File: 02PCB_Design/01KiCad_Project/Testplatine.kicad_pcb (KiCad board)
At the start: 4 copper layers, 210.4 x 100 mm, 137 parts, among them J1 MTSW-104-22-L-D-265-RA, J2 Screw_Terminal_01x03, J3 FCR7350R, J4 FCR7350R, J5 DE9_Receptacle_MountingHoles, J6 MTSW-104-22-L-D-265-RA, J7 Conn_01x06_Pin, U1 AS5047P-ATSM, U10 INA240A1PW, U11 NUCLEO-G431RB, U12 MCP2562FD, U2 ISM330BXTR, U3 L6982, U4 AP2114D, U5 LMG2100R044RARR, U6 INA240A1PW, U7 LMG2100R044RARR, U8 INA240A1PW, U9 LMG2100R044RARR

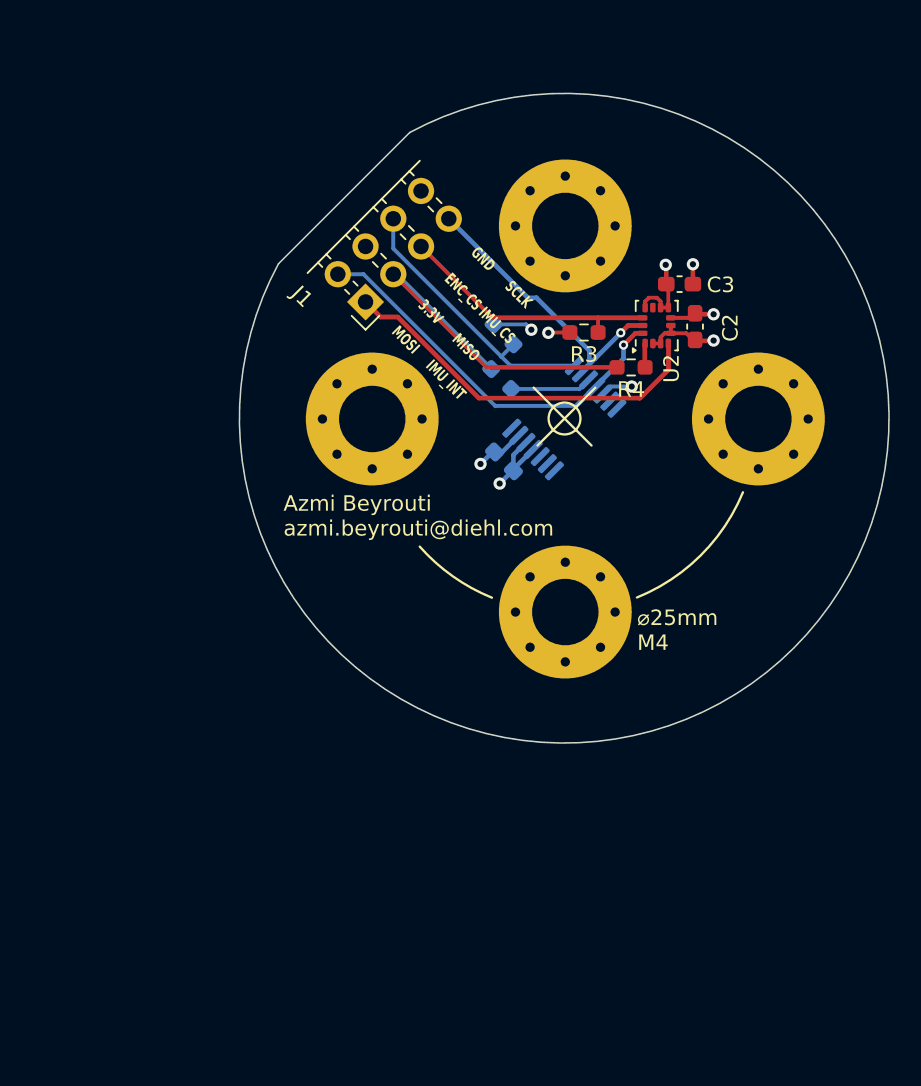
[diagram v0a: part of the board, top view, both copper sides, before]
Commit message: Changed Some Capacitor Sizes, Added Capacitors in Power Gen
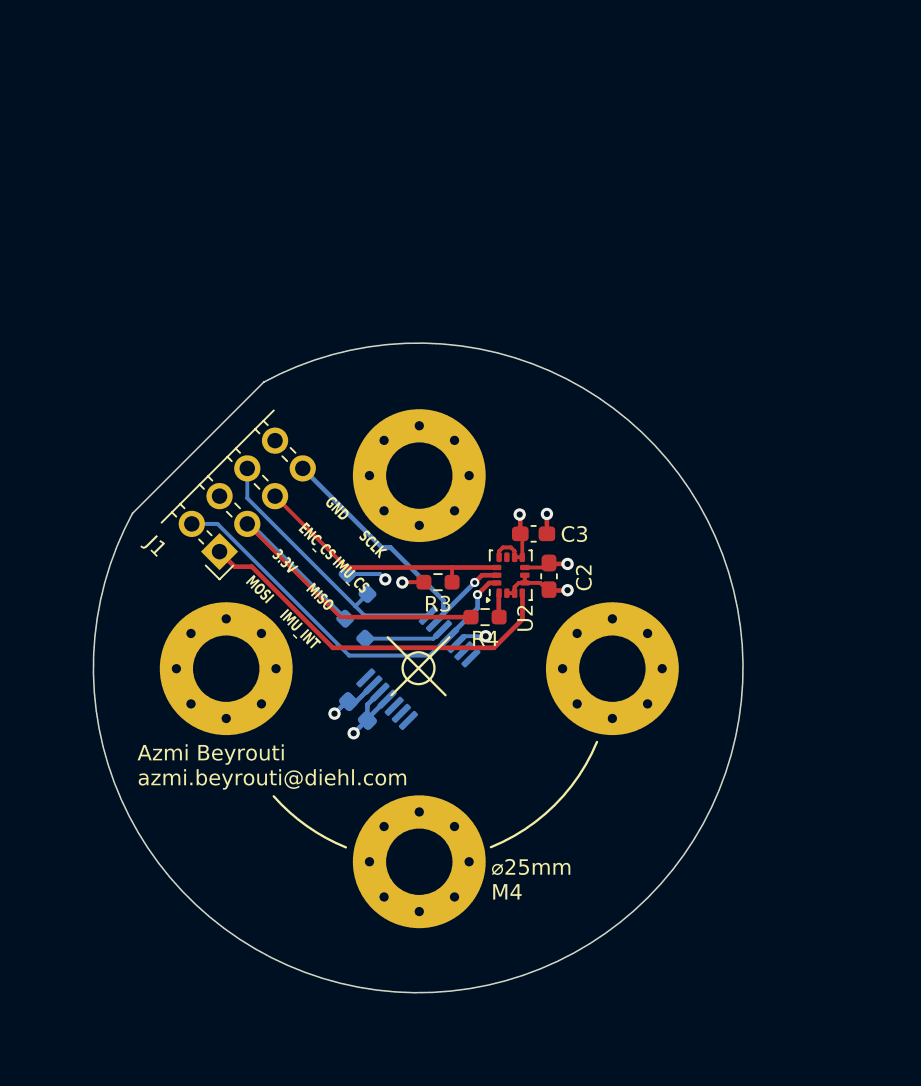
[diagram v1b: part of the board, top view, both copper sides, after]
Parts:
- moved C1 18.7 mm to (219.8, 113.0)
- moved C2 18.7 mm to (232.2, 104.3)
- moved C3 18.7 mm to (231.2, 101.6)
- moved H1 18.7 mm to (223.8, 97.8)
- moved H2 18.7 mm to (223.8, 122.8)
- moved H3 18.7 mm to (236.3, 110.3)
- moved H4 18.7 mm to (211.3, 110.3)
- moved R1 18.7 mm to (219.8, 104.8)
- moved R2 18.7 mm to (219.6, 107.7)
- moved R4 18.7 mm to (228.0, 107.0)
- moved U1 18.7 mm to (223.7, 110.2)
- moved J1 18.7 mm to (210.8, 102.7)
- moved R3 18.7 mm to (225.0, 104.7)
- moved U2 18.7 mm to (229.7, 104.2)
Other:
- board size 210.4 x 100 mm -> 201 x 100 mm

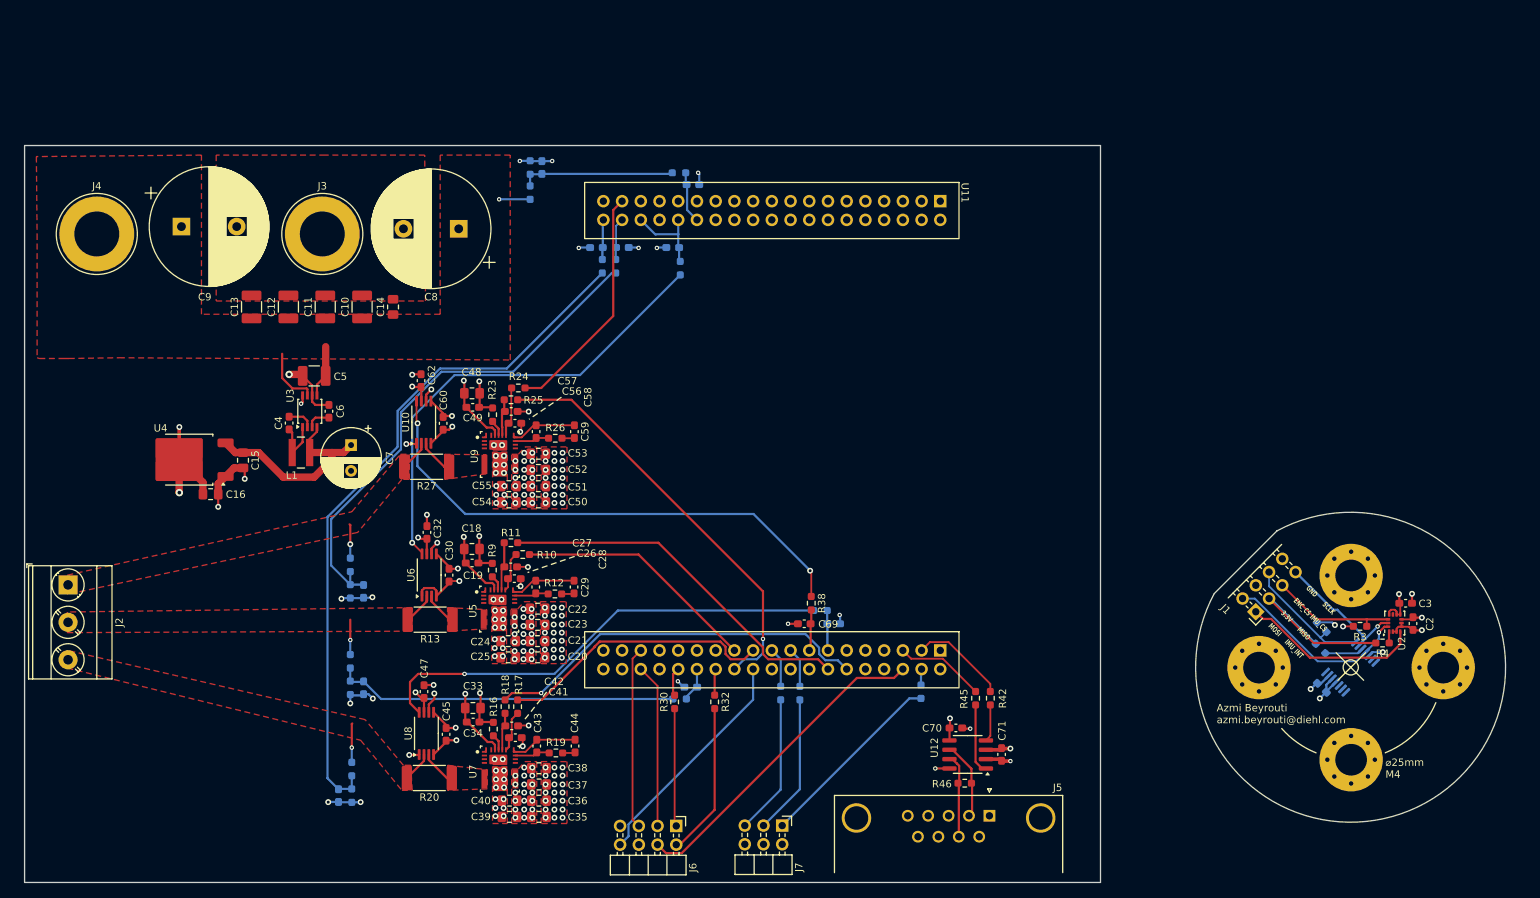
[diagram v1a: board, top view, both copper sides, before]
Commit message: Reworked Half-Bridge and Power-Gen
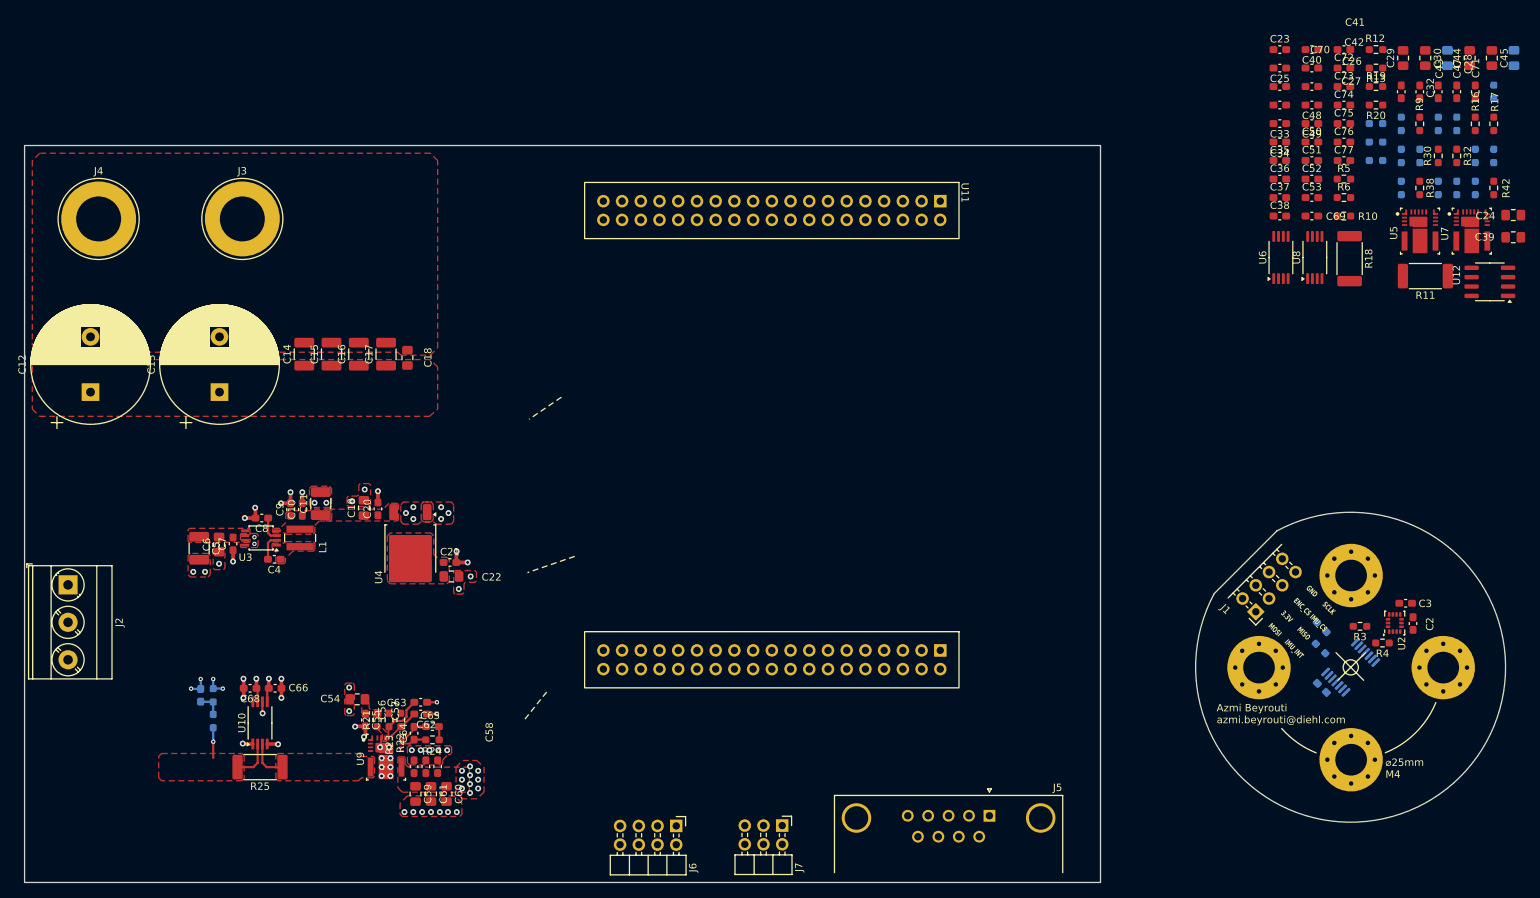
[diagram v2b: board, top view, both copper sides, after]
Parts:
- removed R45: 0R, Resistor_SMD:R_0603_1608Metric_Pad0.98x0.95mm_HandSolder
- removed R46: 120, Resistor_SMD:R_0603_1608Metric_Pad0.98x0.95mm_HandSolder
- added C72: 2.2nF, Capacitor_SMD:C_0603_1608Metric_Pad1.08x0.95mm_HandSolder, F.Cu at (222.8, 28.9)
- added C73: 2.2nF, Capacitor_SMD:C_0603_1608Metric_Pad1.08x0.95mm_HandSolder, F.Cu at (222.8, 31.4)
- added C74: 2.2nF, Capacitor_SMD:C_0603_1608Metric_Pad1.08x0.95mm_HandSolder, F.Cu at (222.8, 34.0)
- added C75: 2.2nF, Capacitor_SMD:C_0603_1608Metric_Pad1.08x0.95mm_HandSolder, F.Cu at (222.8, 36.5)
- added C76: 0.1uF, Capacitor_SMD:C_0603_1608Metric_Pad1.08x0.95mm_HandSolder, F.Cu at (222.8, 39.0)
- added C77: 0.1uF, Capacitor_SMD:C_0603_1608Metric_Pad1.08x0.95mm_HandSolder, F.Cu at (222.8, 41.5)
- added R5: 100k, Resistor_SMD:R_0603_1608Metric_Pad0.98x0.95mm_HandSolder, F.Cu at (222.8, 44.0)
- added R6: 4.22k, Resistor_SMD:R_0603_1608Metric_Pad0.98x0.95mm_HandSolder, F.Cu at (222.8, 46.5)
- C10: value 10uF -> 1uF; footprint Capacitor_SMD:C_1210_3225Metric_Pad1.33x2.70mm_HandSolder -> Capacitor_SMD:C_0603_1608Metric_Pad1.08x0.95mm_HandSolder
- C11: value 10uF -> 47uF
- C12, C13: value 10uF -> 470uF; footprint Capacitor_SMD:C_1210_3225Metric_Pad1.33x2.70mm_HandSolder -> Capacitor_THT:CP_Radial_D16.0mm_P7.50mm
- C14, C15, C16: value 4.7uF -> 10uF; footprint Capacitor_SMD:C_0805_2012Metric_Pad1.18x1.45mm_HandSolder -> Capacitor_SMD:C_1210_3225Metric_Pad1.33x2.70mm_HandSolder
- C17: value 33nF -> 10uF; footprint Capacitor_SMD:C_0603_1608Metric_Pad1.08x0.95mm_HandSolder -> Capacitor_SMD:C_1210_3225Metric_Pad1.33x2.70mm_HandSolder; moved to F.Cu
- C18: value 2.2uF -> 4.7uF
- C19: value 0.1uF -> 4.7uF; footprint Capacitor_SMD:C_0603_1608Metric_Pad1.08x0.95mm_HandSolder -> Capacitor_SMD:C_0805_2012Metric_Pad1.18x1.45mm_HandSolder
- C20, C21: value 220nF -> 100nF; footprint Capacitor_SMD:C_0805_2012Metric_Pad1.18x1.45mm_HandSolder -> Capacitor_SMD:C_0603_1608Metric_Pad1.08x0.95mm_HandSolder
- C22: value 220nF -> 4.7uF
- C23: value 1uF -> 33nF; footprint Capacitor_SMD:C_0805_2012Metric_Pad1.18x1.45mm_HandSolder -> Capacitor_SMD:C_0603_1608Metric_Pad1.08x0.95mm_HandSolder
- C24, C39, C54: value 1uF -> 2.2uF
- C25, C38, C40, C53, C55: value 1uF -> 0.1uF; footprint Capacitor_SMD:C_0805_2012Metric_Pad1.18x1.45mm_HandSolder -> Capacitor_SMD:C_0603_1608Metric_Pad1.08x0.95mm_HandSolder
- C26, C27, C41, C42, C56, C57: value 47p -> 220nF
- C28, C43, C58: value 0.1uF -> 220nF
- C29, C30, C44, C45, C59, C60: value 0.1uF -> 1uF; footprint Capacitor_SMD:C_0603_1608Metric_Pad1.08x0.95mm_HandSolder -> Capacitor_SMD:C_0805_2012Metric_Pad1.18x1.45mm_HandSolder
- C31, C46: value 33nF -> 1uF; footprint Capacitor_SMD:C_0603_1608Metric_Pad1.08x0.95mm_HandSolder -> Capacitor_SMD:C_0805_2012Metric_Pad1.18x1.45mm_HandSolder
- C32, C47, C62: value 0.1uF -> 47p
- C33, C48: value 2.2uF -> 47p; footprint Capacitor_SMD:C_0805_2012Metric_Pad1.18x1.45mm_HandSolder -> Capacitor_SMD:C_0603_1608Metric_Pad1.08x0.95mm_HandSolder
- C35, C36, C50, C51: value 220nF -> 0.1uF; footprint Capacitor_SMD:C_0805_2012Metric_Pad1.18x1.45mm_HandSolder -> Capacitor_SMD:C_0603_1608Metric_Pad1.08x0.95mm_HandSolder
- C37, C52: value 220nF -> 33nF; footprint Capacitor_SMD:C_0805_2012Metric_Pad1.18x1.45mm_HandSolder -> Capacitor_SMD:C_0603_1608Metric_Pad1.08x0.95mm_HandSolder
- C6: footprint Capacitor_SMD:C_0603_1608Metric_Pad1.08x0.95mm_HandSolder -> Capacitor_SMD:C_0805_2012Metric_Pad1.18x1.45mm_HandSolder
- C61: value 33nF -> 1uF; footprint Capacitor_SMD:C_0603_1608Metric_Pad1.08x0.95mm_HandSolder -> Capacitor_SMD:C_0805_2012Metric_Pad1.18x1.45mm_HandSolder; moved to F.Cu
- C63: value 2.2nF -> 47p; moved to F.Cu
- C64, C65, C66, C68: value 2.2nF -> 0.1uF; moved to F.Cu
- C67: value 2.2nF -> 33nF
- C7: value 47uF -> 100nF; footprint Capacitor_THT:CP_Radial_D8.0mm_P3.50mm -> Capacitor_SMD:C_0603_1608Metric_Pad1.08x0.95mm_HandSolder
- C70, C71: value 0.1uF -> 2.2nF
- C8: value 470uF -> 1uF; footprint Capacitor_THT:CP_Radial_D16.0mm_P7.50mm -> Capacitor_SMD:C_0603_1608Metric_Pad1.08x0.95mm_HandSolder
- C9: value 470uF -> 100nF; footprint Capacitor_THT:CP_Radial_D16.0mm_P7.50mm -> Capacitor_SMD:C_0603_1608Metric_Pad1.08x0.95mm_HandSolder
- R10, R17, R24: value 20 -> 10R
- R11, R18, R25: value 20 -> 3.3m; footprint Resistor_SMD:R_0603_1608Metric_Pad0.98x0.95mm_HandSolder -> Resistor_SMD:R_2512_6332Metric_Pad1.40x3.35mm_HandSolder
- R12, R19: value 3R -> 100k
- R13, R20: value 3.3m -> 4.22k; footprint Resistor_SMD:R_2512_6332Metric_Pad1.40x3.35mm_HandSolder -> Resistor_SMD:R_0603_1608Metric_Pad0.98x0.95mm_HandSolder
- R14, R7: value 100k -> 10R
- R15, R8: value 4.22k -> 20
- R16, R23, R9: value 3R -> 20
- R21: value 100k -> 10R; moved to F.Cu
- R22: value 4.22k -> 20; moved to F.Cu
- R26: value 3R -> 100k; moved to B.Cu
- R27: value 3.3m -> 4.22k; footprint Resistor_SMD:R_2512_6332Metric_Pad1.40x3.35mm_HandSolder -> Resistor_SMD:R_0603_1608Metric_Pad0.98x0.95mm_HandSolder; moved to B.Cu
- R28: value 100k -> 33R
- R29: value 4.22k -> 20R
- R32: value 33R -> 20R
- R37, R38: value 20R -> 33R
- R40, R41: value 33R -> 0R
- R42: value 0R -> 120
- moved C46 188.3 mm to (245.9, 27.6)
- moved C31 170.1 mm to (236.8, 27.6)
- moved C45 169.0 mm to (242.9, 27.6)
- moved R15 168.5 mm to (238.1, 36.5)
- moved R14 164.7 mm to (235.6, 36.5)
- moved C47 162.1 mm to (238.1, 32.2)
- moved R20 157.6 mm to (227.1, 34.0)
- moved C39 157.3 mm to (245.8, 51.9)
- moved R29 156.7 mm to (233.1, 40.9)
- moved R16 156.5 mm to (240.6, 36.5)
- moved R17 154.3 mm to (243.1, 36.5)
- moved C44 153.1 mm to (239.8, 27.6)
- moved R28 153.0 mm to (230.6, 40.9)
- moved C43 151.2 mm to (235.6, 32.2)
- moved U7 150.7 mm to (240.1, 51.1)
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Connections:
- C10 pad 1: +24V -> +5V
- C11 pad 1: +24V -> +5V
- C15 pad 1: +5V -> +24V
- C16 pad 1: +3.3V -> +24V
- C17 pad 1: /escSheet/NucleoMorpho/VOLTAGE_BUS -> +24V
- C18 pad 1: +5V -> +24V
- C20 pad 1: +24V -> +5V
- C21 pad 1: +24V -> +3.3V
- C22 pad 1: +24V -> +3.3V
- C23 pad 1: +24V -> /escSheet/NucleoMorpho/VOLTAGE_BUS
- C24 pad 1: +24V -> +5V
- C25 pad 1: +24V -> +5V
- C26 pad 1: Net-(U5-HI) -> +24V
- C27 pad 1: Net-(U5-LI) -> +24V
- C28 pad 1: Net-(U5-HB) -> +24V
- C28 pad 2: Net-(U5-HS) -> GNDA
- C29 pad 1: Net-(C29-Pad1) -> +24V
- C29 pad 2: Net-(U5-HS) -> GNDA
- C30 pad 1: +3.3V -> +24V
- C31 pad 1: /escSheet/HalfBridgePowerStage1/V_PHASE -> +24V
- C32 pad 1: +3.3V -> Net-(U5-HI)
- C33 pad 1: +5V -> Net-(U5-LI)
- C34 pad 1: +5V -> Net-(U5-HB)
- C34 pad 2: GNDA -> Net-(U5-HS)
- C35 pad 1: +24V -> Net-(C35-Pad1)
- C35 pad 2: GNDA -> Net-(U5-HS)
- C36 pad 1: +24V -> +3.3V
- C37 pad 1: +24V -> /escSheet/HalfBridgePowerStage1/V_PHASE
- C38 pad 1: +24V -> +3.3V
- C39 pad 1: +24V -> +5V
- C40 pad 1: +24V -> +5V
- C41 pad 1: Net-(U7-HI) -> +24V
- C42 pad 1: Net-(U7-LI) -> +24V
- C43 pad 1: Net-(U7-HB) -> +24V
- C43 pad 2: Net-(U7-HS) -> GNDA
- C44 pad 1: Net-(C44-Pad1) -> +24V
- C44 pad 2: Net-(U7-HS) -> GNDA
- C45 pad 1: +3.3V -> +24V
- C46 pad 1: /escSheet/HalfBridgePowerStage2/V_PHASE -> +24V
- C47 pad 1: +3.3V -> Net-(U7-HI)
- C48 pad 1: +5V -> Net-(U7-LI)
- C49 pad 1: +5V -> Net-(U7-HB)
- C49 pad 2: GNDA -> Net-(U7-HS)
- C50 pad 1: +24V -> Net-(C50-Pad1)
- C50 pad 2: GNDA -> Net-(U7-HS)
- C51 pad 1: +24V -> +3.3V
- C52 pad 1: +24V -> /escSheet/HalfBridgePowerStage2/V_PHASE
- C53 pad 1: +24V -> +3.3V
- C54 pad 1: +24V -> +5V
- C55 pad 1: +24V -> +5V
- C56 pad 1: Net-(U9-HI) -> +24V
- C57 pad 1: Net-(U9-LI) -> +24V
- C58 pad 1: Net-(U9-HB) -> +24V
- C58 pad 2: Net-(U9-HS) -> GNDA
- C59 pad 1: Net-(C59-Pad1) -> +24V
- C59 pad 2: Net-(U9-HS) -> GNDA
- C6 pad 1: Net-(U3-VCC) -> GNDA
- C6 pad 2: GNDA -> +24V
- C60 pad 1: +3.3V -> +24V
- C61 pad 1: /escSheet/HalfBridgePowerStage3/V_PHASE -> +24V
- C62 pad 1: +3.3V -> Net-(U9-HI)
- C63 pad 1: Net-(U11A-PB14) -> Net-(U9-LI)
- C64 pad 1: Net-(U11A-PC0/PA15) -> Net-(U9-HB)
- C64 pad 2: GNDA -> Net-(U9-HS)
- C65 pad 1: Net-(U11A-PC1/PB9) -> Net-(C65-Pad1)
- C65 pad 2: GNDA -> Net-(U9-HS)
- C66 pad 1: Net-(U11A-PA0) -> +3.3V
- C67 pad 1: Net-(U11A-PA1) -> /escSheet/HalfBridgePowerStage3/V_PHASE
- C68 pad 1: Net-(U11A-PA6) -> +3.3V
- C69 pad 1: Net-(U11A-PA7) -> Net-(U11A-PB14)
- C7 pad 1: +5V -> GNDA
- C7 pad 2: GNDA -> +24V
- C70 pad 1: GNDA -> Net-(U11A-PC0/PA15)
- C70 pad 2: +3.3V -> GNDA
- C71 pad 1: +5V -> Net-(U11A-PC1/PB9)
- C8 pad 1: +24V -> Net-(U3-VCC)
- C9 pad 1: +24V -> +5V
- R10 pad 1: /escSheet/HalfBridgePowerStage1/PWM_HI -> Net-(U5-HB)
- R10 pad 2: Net-(U5-HI) -> Net-(C35-Pad1)
- R11 pad 1: /escSheet/HalfBridgePowerStage1/PWM_LI -> /escSheet/HalfBridgePowerStage1/SW
- R11 pad 2: Net-(U5-LI) -> /escSheet/HalfBridgePowerStage1/PH_OUT
- R12 pad 1: Net-(U5-HB) -> /escSheet/HalfBridgePowerStage1/PH_OUT
- R12 pad 2: Net-(C29-Pad1) -> /escSheet/HalfBridgePowerStage1/V_PHASE
- R13 pad 1: /escSheet/HalfBridgePowerStage1/SW -> /escSheet/HalfBridgePowerStage1/V_PHASE
- R13 pad 2: /escSheet/HalfBridgePowerStage1/PH_OUT -> GNDA
- R14 pad 1: /escSheet/HalfBridgePowerStage1/PH_OUT -> Net-(U7-VCC)
- R14 pad 2: /escSheet/HalfBridgePowerStage1/V_PHASE -> +5V
- R15 pad 1: /escSheet/HalfBridgePowerStage1/V_PHASE -> /escSheet/HalfBridgePowerStage2/PWM_HI
- R15 pad 2: GNDA -> Net-(U7-HI)
- R16 pad 1: Net-(U7-VCC) -> /escSheet/HalfBridgePowerStage2/PWM_LI
- R16 pad 2: +5V -> Net-(U7-LI)
- R17 pad 1: /escSheet/HalfBridgePowerStage2/PWM_HI -> Net-(U7-HB)
- R17 pad 2: Net-(U7-HI) -> Net-(C50-Pad1)
- R18 pad 1: /escSheet/HalfBridgePowerStage2/PWM_LI -> /escSheet/HalfBridgePowerStage2/SW
- R18 pad 2: Net-(U7-LI) -> /escSheet/HalfBridgePowerStage2/PH_OUT
- R19 pad 1: Net-(U7-HB) -> /escSheet/HalfBridgePowerStage2/PH_OUT
- R19 pad 2: Net-(C44-Pad1) -> /escSheet/HalfBridgePowerStage2/V_PHASE
- R20 pad 1: /escSheet/HalfBridgePowerStage2/SW -> /escSheet/HalfBridgePowerStage2/V_PHASE
- R20 pad 2: /escSheet/HalfBridgePowerStage2/PH_OUT -> GNDA
- R21 pad 1: /escSheet/HalfBridgePowerStage2/PH_OUT -> Net-(U9-VCC)
- R21 pad 2: /escSheet/HalfBridgePowerStage2/V_PHASE -> +5V
- R22 pad 1: /escSheet/HalfBridgePowerStage2/V_PHASE -> /escSheet/HalfBridgePowerStage3/PWM_HI
- R22 pad 2: GNDA -> Net-(U9-HI)
- R23 pad 1: Net-(U9-VCC) -> /escSheet/HalfBridgePowerStage3/PWM_LI
- R23 pad 2: +5V -> Net-(U9-LI)
- R24 pad 1: /escSheet/HalfBridgePowerStage3/PWM_HI -> Net-(U9-HB)
- R24 pad 2: Net-(U9-HI) -> Net-(C65-Pad1)
- R25 pad 1: /escSheet/HalfBridgePowerStage3/PWM_LI -> /escSheet/HalfBridgePowerStage3/SW
- R25 pad 2: Net-(U9-LI) -> /escSheet/HalfBridgePowerStage3/PH_OUT
- R26 pad 1: Net-(U9-HB) -> /escSheet/HalfBridgePowerStage3/PH_OUT
- R26 pad 2: Net-(C59-Pad1) -> /escSheet/HalfBridgePowerStage3/V_PHASE
- R27 pad 1: /escSheet/HalfBridgePowerStage3/SW -> /escSheet/HalfBridgePowerStage3/V_PHASE
- R27 pad 2: /escSheet/HalfBridgePowerStage3/PH_OUT -> GNDA
- R28 pad 1: /escSheet/HalfBridgePowerStage3/PH_OUT -> /escSheet/Bus_Connectors/SPI_SCLK
- R28 pad 2: /escSheet/HalfBridgePowerStage3/V_PHASE -> Net-(U11A-PB13)
- R29 pad 1: /escSheet/HalfBridgePowerStage3/V_PHASE -> Net-(U11A-PB14)
- R29 pad 2: GNDA -> /escSheet/HalfBridgePowerStage1/V_PHASE
- R30 pad 1: /escSheet/Bus_Connectors/SPI_SCLK -> Net-(U11A-PB15)
- R30 pad 2: Net-(U11A-PB13) -> /escSheet/Bus_Connectors/SPI_MOSI
- R31 pad 1: Net-(U11A-PB14) -> /escSheet/NucleoMorpho/VOLTAGE_BUS
- R31 pad 2: /escSheet/HalfBridgePowerStage1/V_PHASE -> Net-(U11A-PA0)
- R32 pad 1: Net-(U11A-PB15) -> /escSheet/HalfBridgePowerStage1/I_PHASE
- R32 pad 2: /escSheet/Bus_Connectors/SPI_MOSI -> Net-(U11A-PA1)
- R33 pad 1: /escSheet/NucleoMorpho/VOLTAGE_BUS -> Net-(U11A-PC0/PA15)
- R33 pad 2: Net-(U11A-PA0) -> /escSheet/HalfBridgePowerStage2/V_PHASE
- R34 pad 1: /escSheet/HalfBridgePowerStage1/I_PHASE -> Net-(U11A-PC1/PB9)
- R34 pad 2: Net-(U11A-PA1) -> /escSheet/HalfBridgePowerStage3/V_PHASE
- R35 pad 1: Net-(U11A-PC0/PA15) -> /escSheet/HalfBridgePowerStage2/I_PHASE
- R35 pad 2: /escSheet/HalfBridgePowerStage2/V_PHASE -> Net-(U11A-PA6)
- R36 pad 1: Net-(U11A-PC1/PB9) -> /escSheet/HalfBridgePowerStage3/I_PHASE
- R36 pad 2: /escSheet/HalfBridgePowerStage3/V_PHASE -> Net-(U11A-PA7)
- R37 pad 1: /escSheet/HalfBridgePowerStage2/I_PHASE -> /escSheet/Bus_Connectors/O_ENC_A
- R37 pad 2: Net-(U11A-PA6) -> Net-(U11A-PC6)
- R38 pad 1: /escSheet/HalfBridgePowerStage3/I_PHASE -> Net-(U11A-PC7)
- R38 pad 2: Net-(U11A-PA7) -> /escSheet/Bus_Connectors/O_ENC_B
- R39 pad 1: /escSheet/Bus_Connectors/O_ENC_A -> Net-(U11A-PB6)
- R39 pad 2: Net-(U11A-PC6) -> /escSheet/Bus_Connectors/O_ENC_I
- R40 pad 1: Net-(U11A-PC7) -> /escSheet/Bus_Connectors/FDCAN_RX
- R40 pad 2: /escSheet/Bus_Connectors/O_ENC_B -> Net-(U11A-PB8)
- R41 pad 1: Net-(U11A-PB6) -> /escSheet/Bus_Connectors/FDCAN_TX
- R41 pad 2: /escSheet/Bus_Connectors/O_ENC_I -> Net-(U11A-PB9)
- R42 pad 1: /escSheet/Bus_Connectors/FDCAN_RX -> Net-(U12-CANH)
- R42 pad 2: Net-(U11A-PB8) -> Net-(U12-CANL)
- R7 pad 1: +24V -> Net-(U5-VCC)
- R7 pad 2: /escSheet/NucleoMorpho/VOLTAGE_BUS -> +5V
- R8 pad 1: /escSheet/NucleoMorpho/VOLTAGE_BUS -> /escSheet/HalfBridgePowerStage1/PWM_HI
- R8 pad 2: GNDA -> Net-(U5-HI)
- R9 pad 1: Net-(U5-VCC) -> /escSheet/HalfBridgePowerStage1/PWM_LI
- R9 pad 2: +5V -> Net-(U5-LI)
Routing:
- net +5V: track 355.4 -> 0.00 mm, vias 4 -> 0
- net +3.3V: track 320.2 -> 6.63 mm, vias 9 -> 2
- net /escSheet/HalfBridgePowerStage2/V_PHASE: track 95.0 -> 0.00 mm
- net GNDA: track 115.0 -> 35.0 mm, vias 147 -> 57
- net /escSheet/HalfBridgePowerStage3/I_PHASE: track 71.6 -> 0.00 mm, vias 2 -> 0
- net /escSheet/HalfBridgePowerStage3/V_PHASE: track 68.9 -> 3.40 mm
- net /escSheet/HalfBridgePowerStage2/I_PHASE: track 63.4 -> 0.00 mm, vias 1 -> 0
- net /escSheet/HalfBridgePowerStage1/I_PHASE: track 63.3 -> 0.00 mm, vias 1 -> 0
- net /escSheet/HalfBridgePowerStage3/PWM_LI: track 57.2 -> 0.00 mm, vias 1 -> 0
- net /escSheet/HalfBridgePowerStage2/PWM_LI: track 52.5 -> 0.00 mm, vias 1 -> 0
- net /escSheet/HalfBridgePowerStage1/PWM_LI: track 49.7 -> 0.00 mm
- net /escSheet/HalfBridgePowerStage1/V_PHASE: track 46.2 -> 0.00 mm
- net /escSheet/Bus_Connectors/IMU_CS: track 44.1 -> 0.00 mm
- net /escSheet/HalfBridgePowerStage2/PWM_HI: track 37.2 -> 0.00 mm
- net /escSheet/HalfBridgePowerStage1/PWM_HI: track 33.2 -> 0.00 mm
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- added copper zone on F.Cu, net +3.3V
- added copper zone on F.Cu, net +5V
- added copper zone on F.Cu, net Net-(U3-SW)
- added copper zone on F.Cu, net Net-(U9-VCC)
- removed copper zone on In2.Cu, net +24V
- removed copper zone on In2.Cu, net +3.3VP
- removed copper zone on F.Cu, net /escSheet/HalfBridgePowerStage1/PH_OUT
- removed copper zone on F.Cu, net /escSheet/HalfBridgePowerStage1/SW
- removed copper zone on F.Cu, net /escSheet/HalfBridgePowerStage2/PH_OUT
- removed copper zone on F.Cu, net /escSheet/HalfBridgePowerStage2/SW
